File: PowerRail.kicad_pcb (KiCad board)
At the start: 2 copper layers, 25.4 x 25.4 mm, 20 parts, among them P1 PIN, P2 POUT, U1 ADP5071

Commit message: Slight changes. Note: Need to add a net-tie
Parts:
- C1: value 10.0uF -> 22.0uF; footprint Capacitors_SMD:C_0603_HandSoldering -> Capacitors_SMD:C_1206_HandSoldering
- C6, C7: footprint Capacitors_SMD:C_0805_HandSoldering -> Capacitors_SMD:C_1206_HandSoldering
- P1: footprint Pin_Headers:Pin_Header_Straight_1x02 -> Sockets_MOLEX_KK-System:Socket_MOLEX-KK-RM2-54mm_Lock_2pin_straight
- P2: footprint Pin_Headers:Pin_Header_Straight_1x03 -> Sockets_MOLEX_KK-System:Socket_MOLEX-KK-RM2-54mm_Lock_3pin_straight
- R6: value 10.7M -> 1.07M
- moved P2 10.9 mm to (185.7, 74.3), turned to 0 degrees
- moved P1 5.14 mm to (196.3, 83.6), turned to 90 degrees
- moved C6 1.08 mm to (182.2, 78.9)
- moved C7 1.03 mm to (189.1, 78.9)
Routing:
- net /0V: track 29.7 -> 8.15 mm
- net /+12V: track 33.8 -> 19.5 mm
- net /-7V: track 36.4 -> 27.2 mm
- net +5V: track 13.4 -> 20.3 mm
- net (no net): track 1.66 -> 0.00 mm, vias 1 -> 0
- net GND: track 25.4 -> 26.9 mm, vias 8 -> 9
- added copper zone on F.Cu, net /-7V
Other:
- board size 25.4 x 25.4 mm -> 21.6 x 30.5 mm

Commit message: More work
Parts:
- added T1: NET-TIE, NetTie:NET-TIE-1mm, F.Cu at (187.2, 87.2)
- P1: footprint Sockets_MOLEX_KK-System:Socket_MOLEX-KK-RM2-54mm_Lock_2pin_straight -> xess:HDR_1x2
- P2: footprint Sockets_MOLEX_KK-System:Socket_MOLEX-KK-RM2-54mm_Lock_3pin_straight -> xess:HDR_1x3
- moved P1 10.4 mm to (193.0, 73.7), turned to 0 degrees
- moved P2 2.87 mm to (182.9, 73.7)
- moved C1 0.85 mm to (190.1, 87.5)
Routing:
- net /0V: track 8.15 -> 24.3 mm
- net /-7V: track 27.2 -> 33.8 mm
- net +5V: track 20.3 -> 26.8 mm
- net /+12V: track 19.5 -> 18.2 mm
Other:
- rule pad_to_mask_clearance: 0.2 -> 0

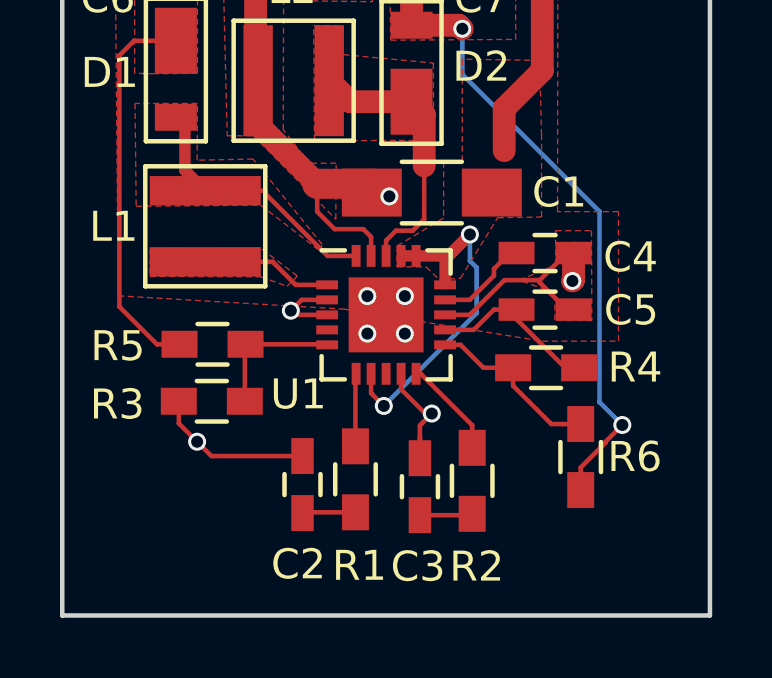
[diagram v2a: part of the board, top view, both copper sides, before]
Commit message: Change wire sizes
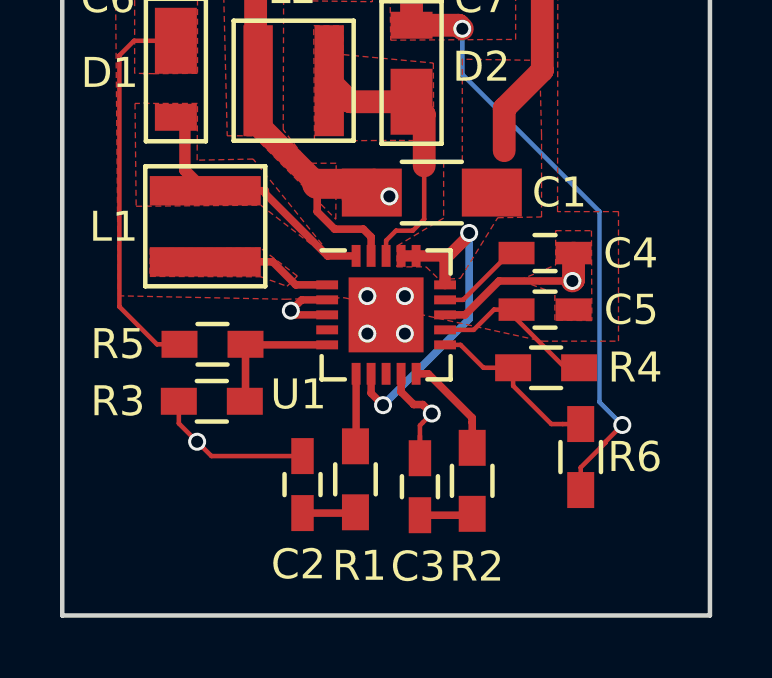
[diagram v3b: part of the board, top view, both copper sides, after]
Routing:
- net +5V: track 26.8 -> 28.7 mm
- net GND: track 27.0 -> 25.8 mm

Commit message: More investigations and calculations
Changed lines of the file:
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@@
-(kicad_pcb (version 4) (host pcbnew "(2015-08-12 BZR 6089)-product")
+(kicad_pcb (version 4) (host pcbnew 0.201509101502+6177~30~ubuntu15.04.1-product)
   (general
     (links 47)
     (no_connects 0)
-    (area 177.724999 71.044999 199.465001 101.675001)
+    (area 163.450001 63.19 214.045715 110.650001)
     (thickness 1.6)
     (drawings 9)
@@
   )
   (setup
-    (last_trace_width 0.254)
+    (last_trace_width 0.25)
     (user_trace_width 0.1524)
     (user_trace_width 0.254)
@@
     (pad_to_mask_clearance 0)
     (aux_axis_origin 0 0)
-    (visible_elements 7FFEFFFF)
+    (visible_elements 7FFFFFFF)
     (pcbplotparams
       (layerselection 0x00030_80000001)
@@
       (effects (font (size 1 1) (thickness 0.15)))
     )
-    (fp_text value 22.0uF (at 0 2.3 180) (layer F.Fab)
+    (fp_text value 22.0uF (at -8.001 -0.127 180) (layer F.Fab)
       (effects (font (size 1 1) (thickness 0.15)))
     )
@@
       (effects (font (size 1 1) (thickness 0.15)))
     )
-    (fp_text value 47nF (at 0 1.9 90) (layer F.Fab)
+    (fp_text value 47nF (at -0.55372 -2.92862 180) (layer F.Fab)
       (effects (font (size 1 1) (thickness 0.15)))
     )
@@
       (effects (font (size 1 1) (thickness 0.15)))
     )
-    (fp_text value 47nF (at 0 1.9 90) (layer F.Fab)
+    (fp_text value 47nF (at -5.5626 0.77724 180) (layer F.Fab)
       (effects (font (size 1 1) (thickness 0.15)))
     )
@@
       (effects (font (size 1 1) (thickness 0.15)))
     )
-    (fp_text value 1.0uF (at 0 1.9) (layer F.Fab)
+    (fp_text value 1.0uF (at 6.13156 0.01524) (layer F.Fab)
       (effects (font (size 1 1) (thickness 0.15)))
     )
@@
       (effects (font (size 1 1) (thickness 0.15)))
     )
-    (fp_text value 1.0uF (at 0 1.9 180) (layer F.Fab)
+    (fp_text value 1.0uF (at -6.13156 -0.03556 180) (layer F.Fab)
       (effects (font (size 1 1) (thickness 0.15)))
     )
@@
       (effects (font (size 1 1) (thickness 0.15)))
     )
-    (fp_text value <40pF@5V (at 0 2 270) (layer F.Fab)
+    (fp_text value <40pF@5V (at 1.54686 5.69214 360) (layer F.Fab)
       (effects (font (size 1 1) (thickness 0.15)))
     )
@@
       (effects (font (size 1 1) (thickness 0.15)))
     )
-    (fp_text value <40pF@5V (at 0 2 90) (layer F.Fab)
+    (fp_text value <40pF@5V (at -1.7145 5.50164 180) (layer F.Fab)
       (effects (font (size 1 1) (thickness 0.15)))
     )
@@
       (effects (font (size 1 1) (thickness 0.15)))
     )
-    (fp_text value 3.3uH (at 0 3.25 90) (layer F.Fab)
+    (fp_text value 3.3uH (at 0 0.31242 180) (layer F.Fab)
       (effects (font (size 1 1) (thickness 0.15)))
     )
@@
       (effects (font (size 1 1) (thickness 0.15)))
     )
-    (fp_text value 6.8uH (at 0 3.25 180) (layer F.Fab)
+    (fp_text value 6.8uH (at 0.09398 1.85928 180) (layer F.Fab)
       (effects (font (size 1 1) (thickness 0.15)))
     )
@@
       (effects (font (size 1 1) (thickness 0.15)))
     )
-    (fp_text value 3.7k (at 0 1.9 270) (layer F.Fab)
+    (fp_text value 3.7k (at 5.80898 0.88392 360) (layer F.Fab)
       (effects (font (size 1 1) (thickness 0.15)))
     )
@@
       (effects (font (size 1 1) (thickness 0.15)))
     )
-    (fp_text value 3.5k (at 0 1.9 270) (layer F.Fab)
+    (fp_text value 3.5k (at 2.58318 -2.8448 360) (layer F.Fab)
       (effects (font (size 1 1) (thickness 0.15)))
     )
@@
       (effects (font (size 1 1) (thickness 0.15)))
     )
-    (fp_text value 100K (at 0 1.9 180) (layer F.Fab)
+    (fp_text value 100K (at 6.89102 -0.15494 180) (layer F.Fab)
       (effects (font (size 1 1) (thickness 0.15)))
     )
@@
       (effects (font (size 1 1) (thickness 0.15)))
     )
-    (fp_text value 100K (at 0 1.9 180) (layer F.Fab)
+    (fp_text value 100K (at -6.096 -0.00254 180) (layer F.Fab)
       (effects (font (size 1 1) (thickness 0.15)))
     )
@@
       (effects (font (size 1 1) (thickness 0.15)))
     )
-    (fp_text value 1.4M (at 0 1.9) (layer F.Fab)
+    (fp_text value 1.4M (at -6.91388 0.14986) (layer F.Fab)
       (effects (font (size 1 1) (thickness 0.15)))
     )
@@
       (effects (font (size 1 1) (thickness 0.15)))
     )
-    (fp_text value 1.07M (at 0 1.9 90) (layer F.Fab)
+    (fp_text value 1.07M (at -1.47066 3.03784 180) (layer F.Fab)
       (effects (font (size 1 1) (thickness 0.15)))
     )
@@
       (effects (font (size 1 1) (thickness 0.15)))
     )
-    (fp_text value 10.0uF (at 0 2.3) (layer F.Fab)
+    (fp_text value 10.0uF (at -6.985 -0.127) (layer F.Fab)
       (effects (font (size 1 1) (thickness 0.15)))
     )
@@
       (effects (font (size 1 1) (thickness 0.15)))
     )
-    (fp_text value 10.0uF (at 0 2.3) (layer F.Fab)
+    (fp_text value 10.0uF (at 6.477 -0.127) (layer F.Fab)
       (effects (font (size 1 1) (thickness 0.15)))
     )
@@
       (effects (font (size 0.8 0.8) (thickness 0.15)))
     )
-    (fp_text value NET-TIE (at 0 0 180) (layer F.Fab) hide
+    (fp_text value NET-TIE (at -0.7112 -1.0541 180) (layer F.Fab)
       (effects (font (size 0.8 0.8) (thickness 0.15)))
     )
@@
   (gr_line (start 177.8 76.2) (end 177.8 71.12) (layer Edge.Cuts) (width 0.15))
   (gr_line (start 177.8 101.6) (end 177.8 76.2) (layer Edge.Cuts) (width 0.15))
+  (segment (start 193.71674 90.42146) (end 193.71674 90.50274) (width 0.1524) (layer F.Cu) (net 0))
   (segment (start 189.59516 89.61454) (end 190.59826 89.61454) (width 0.25) (layer F.Cu) (net 1))
   (segment (start 190.59826 89.61454) (end 191.3636 88.8492) (width 0.25) (layer F.Cu) (net 1))
@@
   (segment (start 189.819001 95.168999) (end 190.119 94.869) (width 0.1524) (layer F.Cu) (net 2))
   (segment (start 189.22016 90.95454) (end 187.97016 90.95454) (width 0.1524) (layer F.Cu) (net 2))
-  (via (at 187.97016 90.95454) (size 0.6) (drill 0.4) (layers F.Cu B.Cu) (net 2))
+  (via (at 187.97016 90.95454) (size 0.6096) (drill 0.3048) (layers F.Cu B.Cu) (net 2))
   (segment (start 189.22016 92.20454) (end 189.22016 90.95454) (width 0.1524) (layer F.Cu) (net 2))
-  (via (at 189.22016 90.95454) (size 0.6) (drill 0.4) (layers F.Cu B.Cu) (net 2))
+  (via (at 189.22016 90.95454) (size 0.6096) (drill 0.3048) (layers F.Cu B.Cu) (net 2))
   (segment (start 187.97016 92.20454) (end 189.22016 92.20454) (width 0.1524) (layer F.Cu) (net 2))
-  (via (at 189.22016 92.20454) (size 0.6) (drill 0.4) (layers F.Cu B.Cu) (net 2))
+  (via (at 189.22016 92.20454) (size 0.6096) (drill 0.3048) (layers F.Cu B.Cu) (net 2))
   (segment (start 187.97016 90.95454) (end 187.97016 92.20454) (width 0.1524) (layer F.Cu) (net 2))
-  (via (at 187.97016 92.20454) (size 0.6) (drill 0.4) (layers F.Cu B.Cu) (net 2))
+  (via (at 187.97016 92.20454) (size 0.6096) (drill 0.3048) (layers F.Cu B.Cu) (net 2))
   (segment (start 185.80862 96.28628) (end 182.77328 96.28628) (width 0.1524) (layer F.Cu) (net 2))
   (segment (start 182.77328 96.28628) (end 182.2958 95.8088) (width 0.1524) (layer F.Cu) (net 2))
@@
   (via (at 182.2958 95.8088) (size 0.6) (drill 0.4) (layers F.Cu B.Cu) (net 2))
   (via (at 185.42 91.44) (size 0.6) (drill 0.4) (layers F.Cu B.Cu) (net 2))
-  (segment (start 193.71674 90.42146) (end 193.71674 90.50274) (width 0.1524) (layer F.Cu) (net 2))
   (segment (start 194.61844 91.40444) (end 194.84344 91.40444) (width 0.1524) (layer F.Cu) (net 2))
   (segment (start 194.61844 89.51976) (end 194.84344 89.51976) (width 0.1524) (layer F.Cu) (net 2))

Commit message: Latest dabbling
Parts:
- added C10: 4.7uF, smd:SM0603, F.Cu at (109.0, 85.5)
- added C11: 6.8pF, smd:SM0603, F.Cu at (102.9, 88.0)
- added C12: 33pF, smd:SM0603, F.Cu at (108.5, 88.0)
- added C13: 10uF, smd:SM0603, F.Cu at (105.5, 85.5)
- added C14: 220pF, Capacitors_SMD:C_0603, F.Cu at (96.5, 72.9)
- added C15: 4.7uF, Capacitors_SMD:C_0603, F.Cu at (99.9, 66.8)
- added C16: 3.9nF, smd:SM0603, F.Cu at (96.9, 99.8)
- added C17: 22.0uF, smd:SM1206, F.Cu at (107.6, 109.0)
- added C18: 12pF, smd:SM0603, F.Cu at (96.9, 102.7)
- added C19: 8.2nF, smd:SM0603, F.Cu at (96.9, 104.2)
- added C20: 68pF, smd:SM0603, F.Cu at (96.9, 107.1)
- added C21: 1.0uF, smd:SM0603, F.Cu at (103.6, 108.8)
- added C22: 1.0uF, smd:SM0603, F.Cu at (102.0, 108.8)
- added C23: 4.7uF, smd:SM0805, F.Cu at (113.5, 97.5)
- added C24: 1.0uF, smd:SM0805, F.Cu at (111.8, 102.0)
- added C25: 10.0uF, smd:SM1206, F.Cu at (115.4, 100.3)
- added C26: 10.0uF, smd:SM1206, F.Cu at (120.0, 103.4)
- added C8: 2.2uF, Capacitors_SMD:C_0603, F.Cu at (112.5, 59.4)
- added C9: 2.2uF, Capacitors_SMD:C_0603, F.Cu at (103.8, 72.9)
- added D3: DFLS240, engstad:diode-smd-powerdi-123, F.Cu at (109.7, 105.0)
- added L3: 47uH, SMD_Packages:SMD-1210_Pol, F.Cu at (106.2, 58.7)
- added L4: 10 uH, engstad:inductor-smd-1212, F.Cu at (106.6, 71.9)
- added L5: 2.2uH, SMD_Packages:SMD-1210_Pol, F.Cu at (102.9, 81.5)
- added L6: 2.2uH, engstad:inductor-smd-xal40, F.Cu at (104.6, 97.3)
- added L7: 3.3uH, SMD_Packages:SMD-1210_Pol, F.Cu at (109.0, 100.6)
- added L8: 0.47uH, SMD_Packages:SMD-1210_Pol, F.Cu at (117.2, 95.4)
- added L9: 1.0uH, SMD_Packages:SMD-1210_Pol, F.Cu at (115.7, 104.6)
- added P3: CONN_01X02, Pin_Headers:Pin_Header_Straight_1x02, F.Cu at (114.8, 85.1)
- added P4: CONN_01X02, Pin_Headers:Pin_Header_Straight_1x02, F.Cu at (97.0, 85.3)
- added P5: CONN_01X02, Pin_Headers:Pin_Header_Straight_1x02, F.Cu at (110.9, 73.7)
- added P6: CONN_01X02, Pin_Headers:Pin_Header_Straight_1x02, F.Cu at (108.3, 66.0)
- added P7: PIN, Pin_Headers:Pin_Header_Angled_1x02, F.Cu at (113.7, 110.4)
- added P8: POUT, Pin_Headers:Pin_Header_Angled_1x03, F.Cu at (122.8, 101.0)
- added R10: 6.98k, smd:SM0603, F.Cu at (99.6, 108.0)
- added R11: 66.5k, smd:SM0603, F.Cu at (101.3, 98.5)
- added R12: 68.1k, smd:SM0603, F.Cu at (99.6, 109.5)
- added R13: 3.09 Ohm, smd:SM0603, F.Cu at (116.0, 98.0)
- added R14: 6.19 Ohm, smd:SM0603, F.Cu at (116.2, 107.0)
- added R7: 21.5k, smd:SM0603, F.Cu at (96.9, 101.2)
- added R8: 5.23k, smd:SM0603, F.Cu at (96.9, 105.7)
- added R9: 4.75k, smd:SM0603, F.Cu at (99.4, 98.5)
- added U2: LMR62014, Housings_SOT-23_SOT-143_TSOT-6:SOT-23-5, F.Cu at (101.1, 71.8)
- added U3: LM3674, Housings_SOT-23_SOT-143_TSOT-6:SOT-23-5, F.Cu at (108.7, 82.5)
- added U4: ADP5071, Housings_DFN_QFN:QFN-20-1EP_4x4mm_Pitch0.5mm, F.Cu at (101.7, 103.4)
- C1: value 22.0uF -> 2.2uF; footprint Capacitors_SMD:C_1206_HandSoldering -> Capacitors_SMD:C_0603
- C2: value 47nF -> 2.2uF; footprint Capacitors_SMD:C_0603_HandSoldering -> Capacitors_SMD:C_0603
- C3: value 47nF -> 4.7pF; footprint Capacitors_SMD:C_0603_HandSoldering -> Capacitors_SMD:C_0603
- C4, C5: value 1.0uF -> 0.1uF; footprint Capacitors_SMD:C_0603_HandSoldering -> Capacitors_SMD:C_0603
- C6: value 10.0uF -> 1.0uF; footprint Capacitors_SMD:C_1206_HandSoldering -> Capacitors_SMD:C_0603
- C7: value 10.0uF -> 10pF; footprint Capacitors_SMD:C_1206_HandSoldering -> Capacitors_SMD:C_0603
- D1: value <40pF@5V -> D_Schottky; footprint camera:PowerDI_123 -> engstad:diode-smd-powerdi-123
- D2: value <40pF@5V -> DFLS240; footprint camera:PowerDI_123 -> engstad:diode-smd-powerdi-123
- L1: value 3.3uH -> 22uH; footprint camera:Inductor_XAL40_SMD -> SMD_Packages:SMD-1210_Pol
- L2: value 6.8uH -> 47uH; footprint camera:Inductor_XAL40_SMD -> SMD_Packages:SMD-1210_Pol
- P1: value PIN -> CONN_01X03; footprint xess:HDR_1x2 -> Pin_Headers:Pin_Header_Straight_1x03
- P2: value POUT -> CONN_01X03; footprint xess:HDR_1x3 -> Pin_Headers:Pin_Header_Straight_1x03
- R1: value 3.7k -> 430k; footprint Resistors_SMD:R_0603_HandSoldering -> Resistors_SMD:R_0603
- R2: value 3.5k -> 280k; footprint Resistors_SMD:R_0603_HandSoldering -> Resistors_SMD:R_0603
- R3: value 100K -> 562k; footprint Resistors_SMD:R_0603_HandSoldering -> smd:SM0603
- R4: value 100K -> 100k; footprint Resistors_SMD:R_0603_HandSoldering -> smd:SM0603
- R5: value 1.4M -> 117k; footprint Resistors_SMD:R_0603_HandSoldering -> Resistors_SMD:R_0603
- R6: value 1.07M -> 13.3k; footprint Resistors_SMD:R_0603_HandSoldering -> Resistors_SMD:R_0603
- T1: footprint NetTie:NET-TIE-1mm -> Oddities:NetTie-I_Connected_SMD; moved to B.Cu
- U1: value ADP5071 -> LT3472; footprint Housings_DFN_QFN:QFN-20-1EP_4x4mm_Pitch0.5mm -> Housings_DFN_QFN:DFN-10-1EP_3x3mm_Pitch0.5mm
- moved P1 99.6 mm to (95.9, 52.1)
- moved R6 99.4 mm to (98.0, 74.7), turned to 0 degrees
- moved C1 95.6 mm to (102.4, 49.5), turned to 0 degrees
- moved R2 91.1 mm to (110.0, 56.5), turned to 90 degrees
- moved C2 90.9 mm to (107.9, 50.3), turned to 180 degrees
- moved L2 90.3 mm to (99.3, 56.8), turned to 270 degrees
- moved U1 89.9 mm to (106.7, 54.5)
- moved C3 89.8 mm to (111.7, 52.8)
- moved R1 89.3 mm to (110.0, 52.9), turned to 90 degrees
- moved R5 88.9 mm to (96.5, 71.1)
- moved L1 88.9 mm to (101.6, 51.9), turned to 0 degrees
- moved C4 88.2 mm to (114.1, 52.0)
- moved C5 87.7 mm to (114.1, 55.1), turned to 0 degrees
- moved R4 87.4 mm to (106.7, 88.0), turned to 90 degrees
- moved T1 82.5 mm to (106.3, 103.3), turned to 90 degrees
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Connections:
- C1 pad 1: +5V -> /Extras/VIN
- C2 pad 1: Net-(C2-Pad1) -> /Extras/+12V
- C3 pad 1: Net-(C3-Pad1) -> /Extras/FB+
- C3 pad 2: GND -> /Extras/+12V
- C4 pad 1: Net-(C4-Pad1) -> /Extras/SS+
- C5 pad 1: GND -> /Extras/SS-
- C5 pad 2: Net-(C5-Pad2) -> GND
- C6 pad 1: /+12V -> Net-(C6-Pad1)
- C6 pad 2: /0V -> /Extras/SW-
- C7 pad 1: /0V -> /Extras/-7V
- C7 pad 2: /-7V -> /Extras/FB-
- D1 pad 1: /+12V -> /Extras/VOUT_12V
- D1 pad 2: Net-(D1-Pad2) -> /Extras/SW3
- D2 pad 1: Net-(D2-Pad1) -> /ADP5071/12V0
- D2 pad 2: /-7V -> /ADP5071/SW1
- L1 pad 1: Net-(L1-Pad1) -> /Extras/VIN
- L1 pad 2: Net-(D1-Pad2) -> /Extras/SW+
- L2 pad 1: Net-(D2-Pad1) -> /Extras/VIN
- L2 pad 2: /0V -> /Extras/SW-
- P1 pad 1: +5V -> /Extras/VIN
- P2 pad 1: /+12V -> /Extras/+12V
- P2 pad 2: /0V -> GND
- P2 pad 3: /-7V -> /Extras/-7V
- R1 pad 1: Net-(R1-Pad1) -> /Extras/FB+
- R1 pad 2: Net-(C2-Pad1) -> /Extras/+12V
- R2 pad 1: Net-(R2-Pad1) -> /Extras/-7V
- R2 pad 2: Net-(C3-Pad1) -> /Extras/FB-
- R3 pad 1: Net-(R3-Pad1) -> /Extras/VOUT_3V3
- R3 pad 2: GND -> /Extras/FB2
- R4 pad 1: Net-(C5-Pad2) -> /Extras/FB2
- R4 pad 2: Net-(R4-Pad2) -> GND
- R5 pad 1: /+12V -> /Extras/VOUT_12V
- R5 pad 2: Net-(R3-Pad1) -> /Extras/FB
- R6 pad 1: /-7V -> /Extras/FB
- R6 pad 2: Net-(R4-Pad2) -> GND
- T1 pad 2: /0V -> /ADP5071/0V
- U1 pad 1: Net-(L1-Pad1) -> /Extras/SW+
- U1 pad 10: Net-(R2-Pad1) -> /Extras/+12V
- U1 pad 11: Net-(R4-Pad2) -> GND
- U1 pad 2: GND -> /Extras/VIN
- U1 pad 3: GND -> /Extras/~SHDN
- U1 pad 4: Net-(U1-Pad4) -> /Extras/SW-
- U1 pad 5: Net-(R3-Pad1) -> Net-(C6-Pad1)
- U1 pad 6: Net-(R1-Pad1) -> /Extras/FB-
- U1 pad 7: +5V -> /Extras/SS-
- U1 pad 8: Net-(U1-Pad8) -> /Extras/FB+
- U1 pad 9: GND -> /Extras/SS+
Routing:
- net /-7V: track 33.8 -> 0.00 mm, vias 2 -> 0
- net GND: track 25.7 -> 53.7 mm, vias 9 -> 23
- net /0V: track 24.3 -> 0.00 mm
- net /ADP5071/0V: track 0.00 -> 21.9 mm, vias 0 -> 1
- net /+12V: track 18.2 -> 0.00 mm
- net /Extras/FB2: track 0.00 -> 17.8 mm, vias 0 -> 2
- net /ADP5071/12V0: track 0.00 -> 16.7 mm
- net /ADP5071/-7V0: track 0.00 -> 14.9 mm, vias 0 -> 2
- net /ADP5071/+12V: track 0.00 -> 12.0 mm
- net /Extras/~SHDN: track 0.00 -> 11.1 mm
- net Net-(D2-Pad1): track 9.20 -> 0.00 mm
- net Net-(D1-Pad2): track 8.84 -> 0.00 mm
- net /ADP5071/SW1: track 0.00 -> 8.78 mm
- net /ADP5071/-7V: track 0.00 -> 8.56 mm
- net /ADP5071/SW2: track 0.00 -> 6.24 mm
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- added copper zone on F.Cu, net /ADP5071/+12V
- added copper zone on F.Cu, net /ADP5071/-7V
- added copper zone on F.Cu, net /ADP5071/-7V0
- added copper zone on F.Cu, net /ADP5071/0V
- added copper zone on F.Cu, net /ADP5071/12V0
- added copper zone on F.Cu, net /ADP5071/INBK
- added copper zone on F.Cu, net /ADP5071/SW1
- added copper zone on F.Cu, net /ADP5071/SW2
- added copper zone on F.Cu, net /Additional/+12V
- added copper zone on F.Cu, net /Additional/-7V
- added copper zone on F.Cu, net /Additional/FB
- added copper zone on F.Cu, net /Additional/FB+
- added copper zone on F.Cu, net /Additional/FB-
- added copper zone on F.Cu, net /Additional/SW+
- added copper zone on F.Cu, net /Additional/SW-
- added copper zone on F.Cu, net /Additional/SW3
- added copper zone on F.Cu, net /Additional/SW4
- added copper zone on F.Cu, net /Additional/VIN
- added copper zone on F.Cu, net /Additional/VIN_2V7_14V0
- added copper zone on F.Cu, net /Additional/VIN_2V7_5V5
- added copper zone on F.Cu, net /Additional/VOUT_12V
- added copper zone on F.Cu, net /Additional/VOUT_3V3
- added copper zone on F.Cu, net Net-(C13-Pad1)
- removed copper zone on F.Cu, net /+12V
- removed copper zone on F.Cu, net /-7V
- removed copper zone on F.Cu, net /0V
- removed copper zone on F.Cu, net Net-(D1-Pad2)
- removed copper zone on F.Cu, net Net-(D2-Pad1)
- removed copper zone on F.Cu, net Net-(L1-Pad1)
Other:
- board size 21.6 x 30.5 mm -> 31.2 x 65.9 mm
- board text added: "GND"
- board text added: "Vin 2.7-5.5V"
- board text added: "Vout 3.3V"

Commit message: Latest work
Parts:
- added C27: 10uF, smd:SM1206, F.Cu at (195.2, 33.1)
- added C28: 10uF, smd:SM1206, F.Cu at (206.0, 43.6)
- added C29: 10uF, smd:SM0805, F.Cu at (201.9, 38.0)
- added C30: 1.0u, smd:SM0603, F.Cu at (192.0, 37.7)
- added C31: 10uF, smd:SM1206, F.Cu at (208.5, 43.6)
- added C32: 10uF, smd:SM1206, F.Cu at (192.0, 34.3)
- added C33: 3.3uF, smd:SM0805, F.Cu at (198.4, 28.6)
- added C34: 4.7u, smd:SM0805, F.Cu at (203.9, 43.5)
- added C35: 10.0u, smd:SM1206, F.Cu at (206.2, 54.6)
- added C36: 0.1u, smd:SM0603, F.Cu at (186.4, 45.4)
- added C37: 10.0u, smd:SM1206, F.Cu at (198.9, 56.4)
- added C38: 0.1u, smd:SM0603, F.Cu at (186.4, 47.6)
- added C39: 47.0u, smd:SM1206, F.Cu at (180.1, 41.4)
- added C40: 47.0u, smd:SM1206, F.Cu at (190.9, 56.5)
- added C41: 22u, smd:SM1206, F.Cu at (195.0, 57.9)
- added C42: 22u, smd:SM1206, F.Cu at (203.6, 56.4)
- added C43: 22u, smd:SM1206, F.Cu at (181.5, 51.3)
- added C44: 22u, smd:SM1206, F.Cu at (184.4, 36.2)
- added C45: 10uF, smd:SM1206, F.Cu at (198.9, 25.4)
- added C46: 22uF, smd:SM1206, F.Cu at (213.1, 52.7)
- added C47: 22uF, smd:SM1206, F.Cu at (210.6, 52.7)
- added C48: 10uF, smd:SM0805, F.Cu at (205.8, 35.2)
- added C49: C_Small, smd:SM0603, F.Cu at (213.6, 46.4)
- added D4: 30V/0.5A, Diodes_SMD:SOD-123, F.Cu at (195.9, 38.6)
- added D5: 30V/0.5A, Diodes_SMD:SOD-123, F.Cu at (205.1, 39.1)
- added D6: 30V/0.5A, Diodes_SMD:SOD-123, F.Cu at (189.6, 37.6)
- added L10: 4.7uH/1.9A, engstad:inductor-smd-40x40, F.Cu at (207.2, 49.5)
- added L11: 12uH, engstad:inductor-smd-4.5x4.5x3.2, F.Cu at (210.2, 37.3)
- added L12: 12uH, engstad:inductor-smd-4.5x4.5x3.2, F.Cu at (200.1, 33.4)
- added L13: 12uH, engstad:inductor-smd-4.5x4.5x3.2, F.Cu at (188.0, 30.5)
- added L14: 4.7uF/1.0A, engstad:inductor-smd-40x40, F.Cu at (202.6, 51.5)
- added L15: 4.7uH/1.9A, engstad:inductor-smd-40x40, F.Cu at (195.3, 54.4)
- added L16: 4.7uH/1.65A, engstad:inductor-smd-40x40, F.Cu at (184.0, 39.9)
- added L17: 3.3uH/3.3A, engstad:inductor-smd-50x50, F.Cu at (185.7, 53.7)
- added P10: LEDS, xess:HDR_1x2, F.Cu at (221.4, 41.2)
- added P11: CONN_01X06, xess:HDR_1x6, F.Cu at (195.4, 67.2)
- added P12: CONN_01X02, xess:HDR_1x2, F.Cu at (212.6, 23.4)
- added P13: USB_OTG, w_conn_pc:conn_usb_B_mini_smd, F.Cu at (179.1, 23.5)
- added P14: CONN_01X06, xess:HDR_1x6, F.Cu at (172.2, 45.5)
- added P15: JTI-PWR, xess:HDR_1x2, F.Cu at (194.2, 22.7)
- added P9: ADJ, xess:HDR_1x1, F.Cu at (216.2, 44.8)
- added R15: 550k, smd:SM0603, F.Cu at (199.5, 37.0)
- added R16: 85.0k, smd:SM0603, F.Cu at (193.6, 40.7)
- added R17: 15.0k, smd:SM0603, F.Cu at (192.0, 39.3)
- added R18: 50.0k, smd:SM0603, F.Cu at (196.5, 40.7)
- added R19: 660k, smd:SM0603, F.Cu at (201.4, 44.4)
- added R20: 10, smd:SM0603, F.Cu at (198.5, 41.5)
- added R21: 10k, smd:SM0603, F.Cu at (213.6, 44.9)
- added R24: 500k, smd:SM0603, F.Cu at (200.0, 39.8)
- added R25: 220k, smd:SM0603, F.Cu at (199.4, 44.9)
- added R26: 100k, smd:SM0603, F.Cu at (200.0, 42.2)
- added R27: 440k, smd:SM0603, F.Cu at (199.0, 50.4)
- added R28: 220k, smd:SM0603, F.Cu at (199.0, 52.0)
- added R29: 820k, smd:SM0603, F.Cu at (183.9, 43.5)
- added R30: 180k, smd:SM0603, F.Cu at (183.9, 45.4)
- added R31: 820k, smd:SM0603, F.Cu at (190.0, 51.2)
- added R32: 180k, smd:SM0603, F.Cu at (191.5, 51.2)
- added R33: 330k, smd:SM0603, F.Cu at (195.0, 50.9)
- added R34: 330k, smd:SM0603, F.Cu at (196.5, 50.9)
- added T2: NET-TIE, Oddities:NetTie-I_Connected_SMD, F.Cu at (224.3, 47.8)
- added U5: TPS65530, Housings_DFN_QFN:UQFN-48-1EP_6x6mm_Pitch0.4mm, F.Cu at (194.0, 45.4)
- added U6: VEC2616, engstad:sot-28fl, F.Cu at (202.5, 46.9)
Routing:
- net /TPS65530/EN_CCD: track 0.00 -> 22.4 mm, vias 0 -> 1
- net /TPS65530/EN_SEQ: track 0.00 -> 17.6 mm, vias 0 -> 1
- net /TPS65530/VOUT_AFE_3V3: track 0.00 -> 16.1 mm
- net /TPS65530/VOUT_IO_3V3: track 0.00 -> 15.4 mm
- net /TPS65530/VCC3: track 0.00 -> 12.5 mm
- net GNDPWR: track 0.00 -> 12.5 mm
- net Net-(L17-Pad1): track 0.00 -> 10.8 mm
- net GND: track 53.7 -> 64.1 mm
- net /TPS65530/VCC2: track 0.00 -> 10.3 mm
- net /TPS65530/VCC1: track 0.00 -> 9.89 mm
- net Net-(R29-Pad2): track 0.00 -> 9.43 mm
- net /TPS65530/VCC4: track 0.00 -> 9.37 mm
- net Net-(L17-Pad2): track 0.00 -> 9.22 mm
- net /TPS65530/SW4S: track 0.00 -> 8.92 mm
- net /TPS65530/SW4I: track 0.00 -> 8.09 mm
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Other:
- board size 31.2 x 65.9 mm -> 125 x 92.4 mm
